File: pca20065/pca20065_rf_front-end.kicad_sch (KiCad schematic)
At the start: 42 parts, among them J1 ${ALTIUM_VALUE}, J2 ${ALTIUM_VALUE}, Q5 ${ALTIUM_VALUE}, U17 QM13345, U22 BGS12xN6

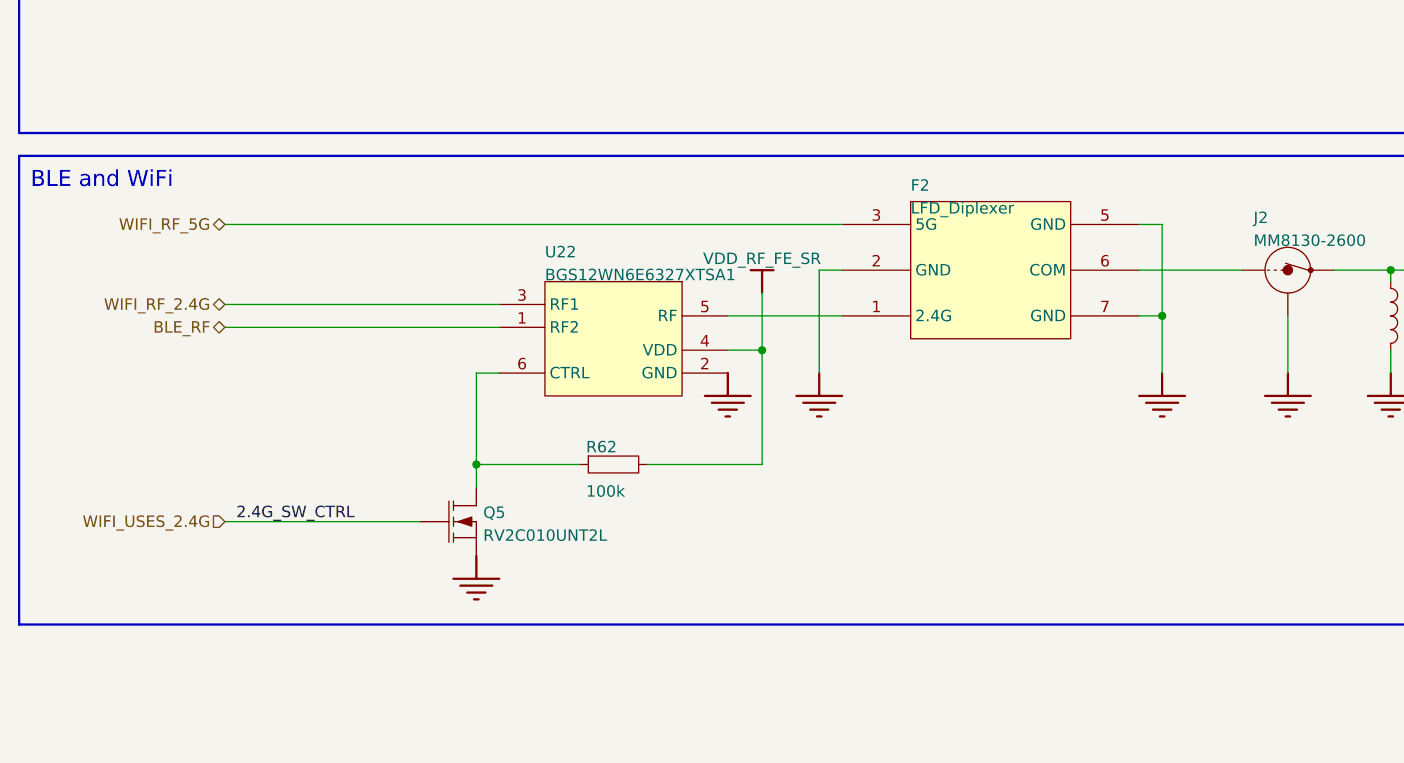
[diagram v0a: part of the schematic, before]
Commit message: Replaced nrf5340 with nrf54l15
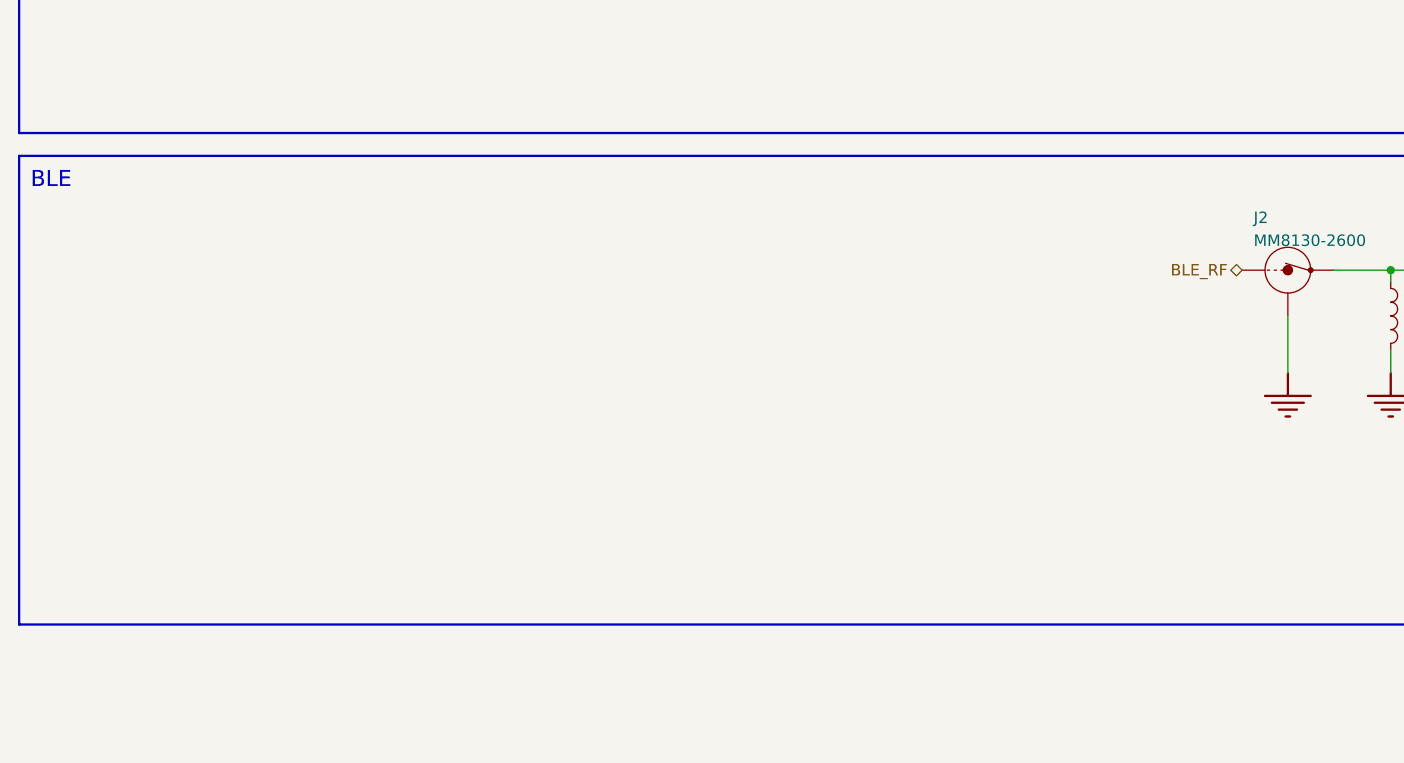
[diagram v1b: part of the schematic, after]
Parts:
- removed F2: LFD_Diplexer, pca20065-import-fps:CAF-50P160X80-6N, symbol pca20065:LFD_Diplexer
- removed Q5: ${ALTIUM_VALUE}, pca20065-import-fps:DFN65P100X40-3L, symbol pca20065:T{colon}FET-N
- removed R62: ${ALTIUM_VALUE}, pca20065-import-fps:RESC0603X03L_C, symbol pca20065:RES_2
- removed U22: BGS12xN6, pca20065-import-fps:TSNP-6-8, symbol pca20065:BGS12xN6
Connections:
- net BLE_RF: now also J2.1 (IN)
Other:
- note added: "BLE"
- note removed: "BLE and WiFi"
